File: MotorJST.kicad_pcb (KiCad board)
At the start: 2 copper layers, 17.5 x 19.5 mm, 2 parts, among them J1 Conn_01x06_Male, J2 Conn_01x06

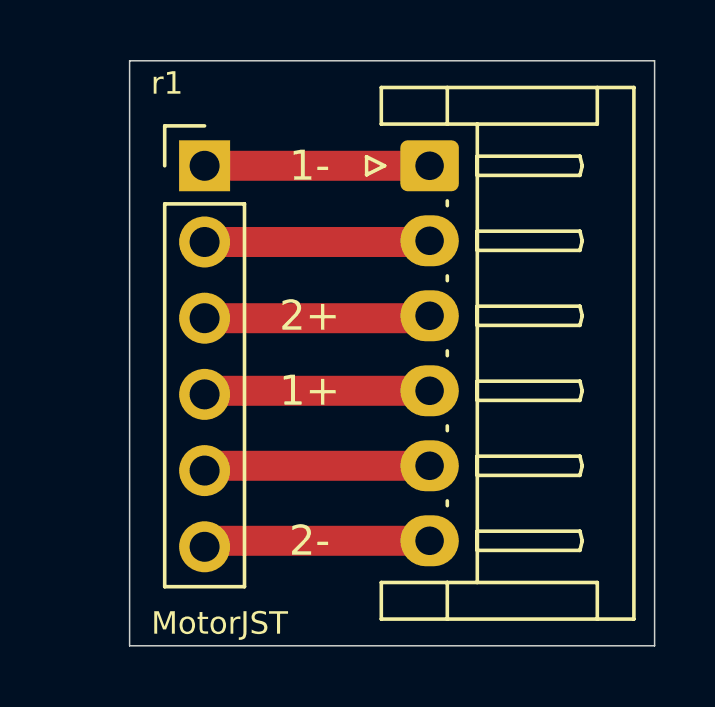
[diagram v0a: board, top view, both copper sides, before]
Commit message: Update traces with more copper.
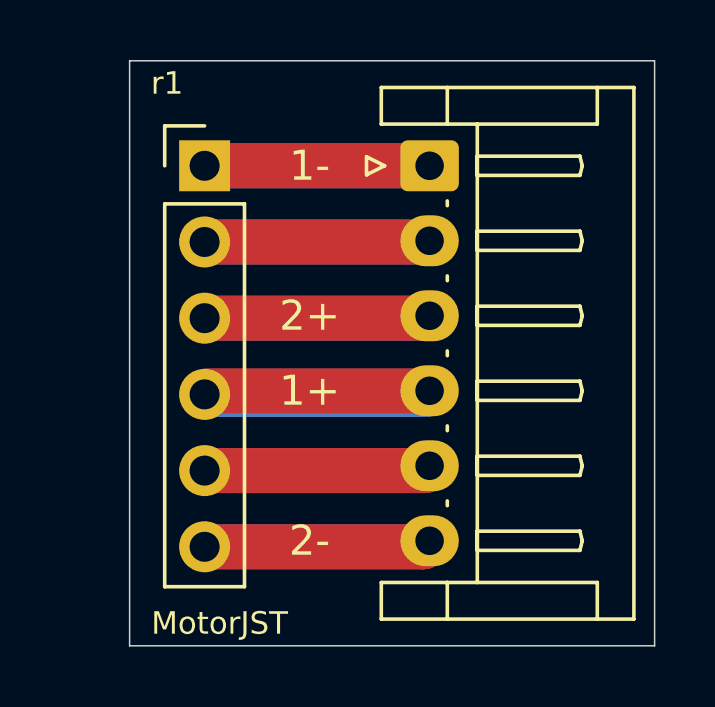
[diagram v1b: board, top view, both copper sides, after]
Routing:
- net Net-(J1-Pad6): track 7.58 -> 15.2 mm
- net Net-(J1-Pad5): track 7.57 -> 15.1 mm
- net Net-(J1-Pad4): track 7.55 -> 15.1 mm
- net Net-(J1-Pad3): track 7.53 -> 15.1 mm
- net Net-(J1-Pad2): track 7.52 -> 15.0 mm
- net Net-(J1-Pad1): track 7.50 -> 15.0 mm
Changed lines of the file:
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@@
     (effects (font (size 0.75 0.75) (thickness 0.1)))
   )
-  (segment (start 204.5 132) (end 197.2 132) (width 1) (layer "F.Cu") (net 1))
-  (segment (start 197.2 132) (end 197 132.2) (width 1) (layer "F.Cu") (net 1))
-  (segment (start 204.5 129.5) (end 197.16 129.5) (width 1) (layer "F.Cu") (net 2))
-  (segment (start 197.16 129.5) (end 197 129.66) (width 1) (layer "F.Cu") (net 2))
+  (segment (start 197 132.2) (end 204.3 132.2) (width 1.5) (layer "F.Cu") (net 1))
+  (segment (start 204.3 132.2) (end 204.5 132) (width 1.5) (layer "F.Cu") (net 1))
+  (segment (start 197 132.2) (end 204.3 132.2) (width 1.5) (layer "B.Cu") (net 1))
+  (segment (start 204.3 132.2) (end 204.5 132) (width 1.5) (layer "B.Cu") (net 1))
+  (segment (start 204.34 129.66) (end 204.5 129.5) (width 1.5) (layer "F.Cu") (net 2))
+  (segment (start 197 129.66) (end 204.34 129.66) (width 1.5) (layer "F.Cu") (net 2))
+  (segment (start 204.34 129.66) (end 204.5 129.5) (width 1.5) (layer "B.Cu") (net 2))
+  (segment (start 197 129.66) (end 204.34 129.66) (width 1.5) (layer "B.Cu") (net 2))
   (segment (start 197.12 127) (end 197 127.12) (width 1) (layer "F.Cu") (net 3))
-  (segment (start 204.5 127) (end 197.12 127) (width 1) (layer "F.Cu") (net 3))
-  (segment (start 197 124.58) (end 204.42 124.58) (width 1) (layer "F.Cu") (net 4))
-  (segment (start 204.42 124.58) (end 204.5 124.5) (width 1) (layer "F.Cu") (net 4))
-  (segment (start 197 122.04) (end 204.46 122.04) (width 1) (layer "F.Cu") (net 5))
-  (segment (start 204.46 122.04) (end 204.5 122) (width 1) (layer "F.Cu") (net 5))
-  (segment (start 197 119.5) (end 204.5 119.5) (width 1) (layer "F.Cu") (net 6))
+  (segment (start 204.5 127) (end 197.12 127) (width 1.5) (layer "F.Cu") (net 3))
+  (segment (start 197 127.12) (end 204.38 127.12) (width 1.5) (layer "B.Cu") (net 3))
+  (segment (start 204.38 127.12) (end 204.5 127) (width 1.5) (layer "B.Cu") (net 3))
+  (segment (start 204.42 124.58) (end 204.5 124.5) (width 1.5) (layer "F.Cu") (net 4))
+  (segment (start 197 124.58) (end 204.42 124.58) (width 1.5) (layer "F.Cu") (net 4))
+  (segment (start 197 124.58) (end 204.42 124.58) (width 1.5) (layer "B.Cu") (net 4))
+  (segment (start 204.42 124.58) (end 204.5 124.5) (width 1.5) (layer "B.Cu") (net 4))
+  (segment (start 204.46 122.04) (end 204.5 122) (width 1.5) (layer "F.Cu") (net 5))
+  (segment (start 197 122.04) (end 204.46 122.04) (width 1.5) (layer "F.Cu") (net 5))
+  (segment (start 204.46 122.04) (end 204.5 122) (width 1.5) (layer "B.Cu") (net 5))
+  (segment (start 197 122.04) (end 204.46 122.04) (width 1.5) (layer "B.Cu") (net 5))
+  (segment (start 197 119.5) (end 204.5 119.5) (width 1.5) (layer "F.Cu") (net 6))
+  (segment (start 197 119.5) (end 204.5 119.5) (width 1.5) (layer "B.Cu") (net 6))
 )

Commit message: Update MotorJST with the correct 2mm pitch connector.
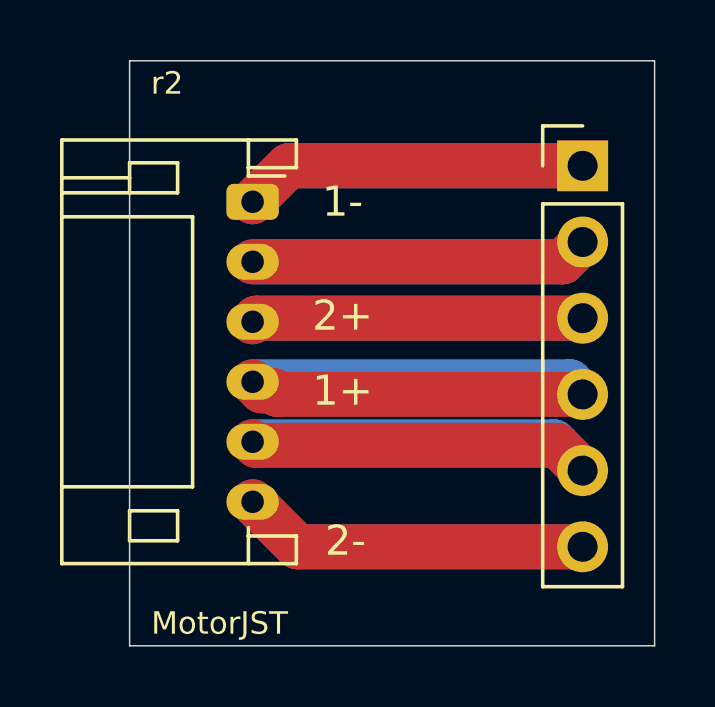
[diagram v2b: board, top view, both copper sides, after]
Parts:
- J1: footprint Connector_JST:JST_EH_S6B-EH_1x06_P2.50mm_Horizontal -> Connector_JST:JST_PH_S6B-PH-K_1x06_P2.00mm_Horizontal
- moved J2 12.6 mm to (209.6, 119.5)
- moved J1 6.02 mm to (198.6, 120.7)
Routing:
- net Net-(J1-Pad6): track 15.2 -> 23.2 mm
- net Net-(J1-Pad1): track 15.0 -> 23.0 mm
- net Net-(J1-Pad5): track 15.1 -> 22.8 mm
- net Net-(J1-Pad2): track 15.0 -> 22.5 mm
- net Net-(J1-Pad4): track 15.1 -> 22.3 mm
- net Net-(J1-Pad3): track 15.1 -> 22.1 mm
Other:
- board text added: "(c) iQury.us Jan 2021"
- board text added: "r2"
- board text removed: "(c) iQury.us Dec 2020"
- board text removed: "r1"
